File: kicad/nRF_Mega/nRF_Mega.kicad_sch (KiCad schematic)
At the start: 11 parts, among them J1 Screw_Terminal_01x02, M1 Motor_Servo, M2 Motor_Servo, M3 Motor_Servo, M4 Motor_Servo, M5 Motor_Servo, U1 NRF24L01_Breakout

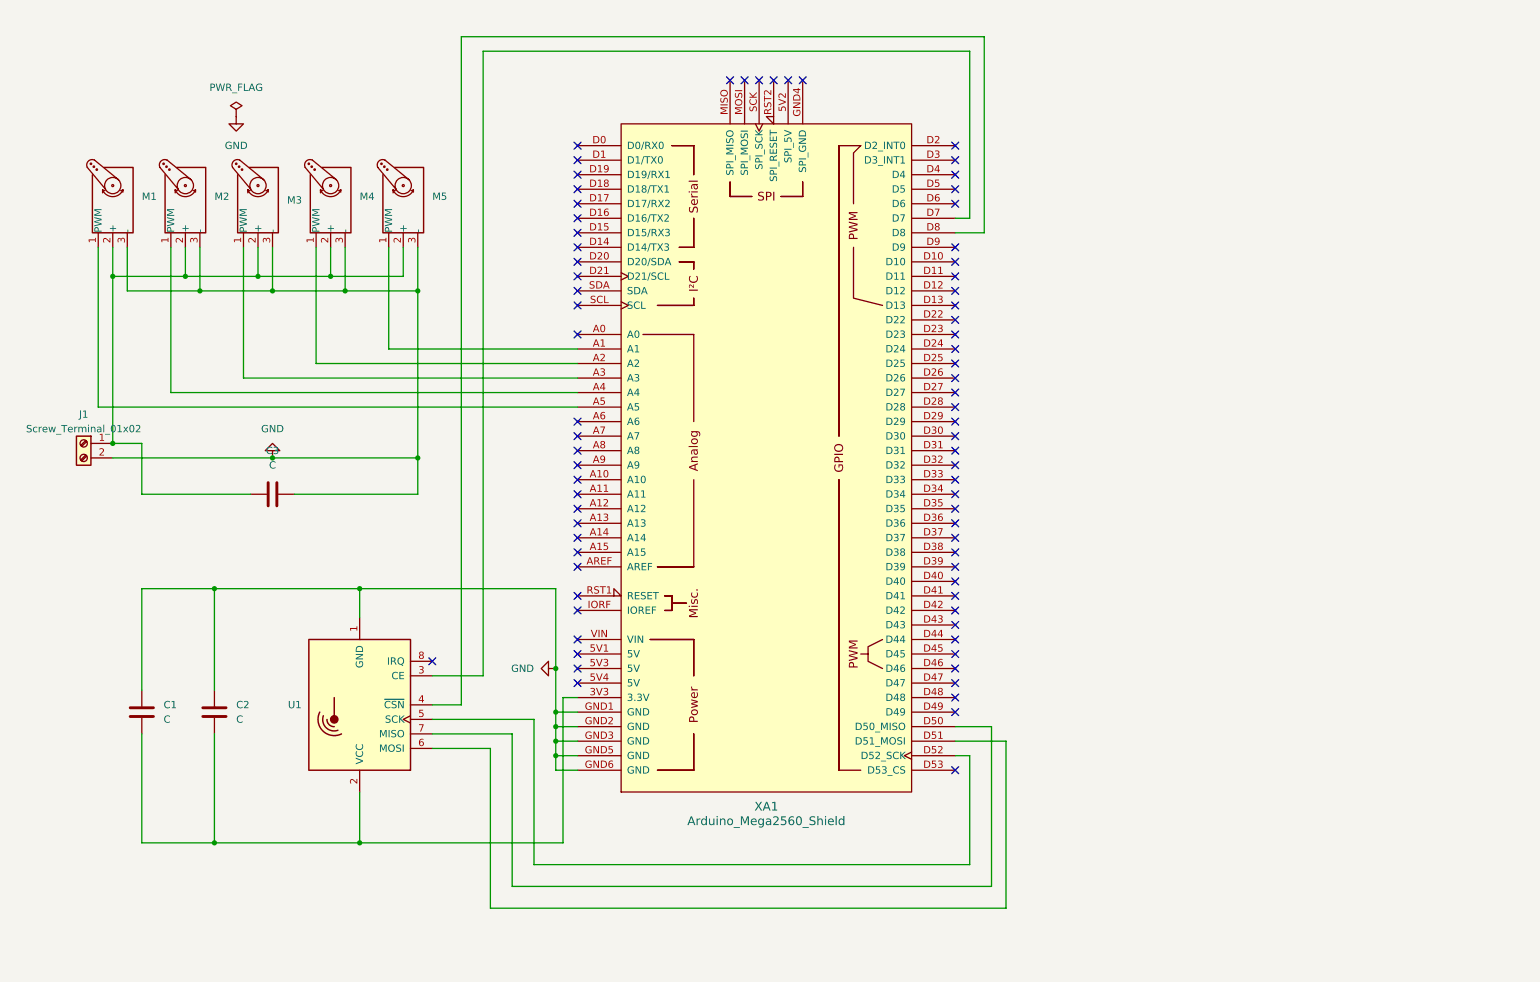
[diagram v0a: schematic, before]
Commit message: corrected nRF placement, minimized wire length, fixed caps and connector
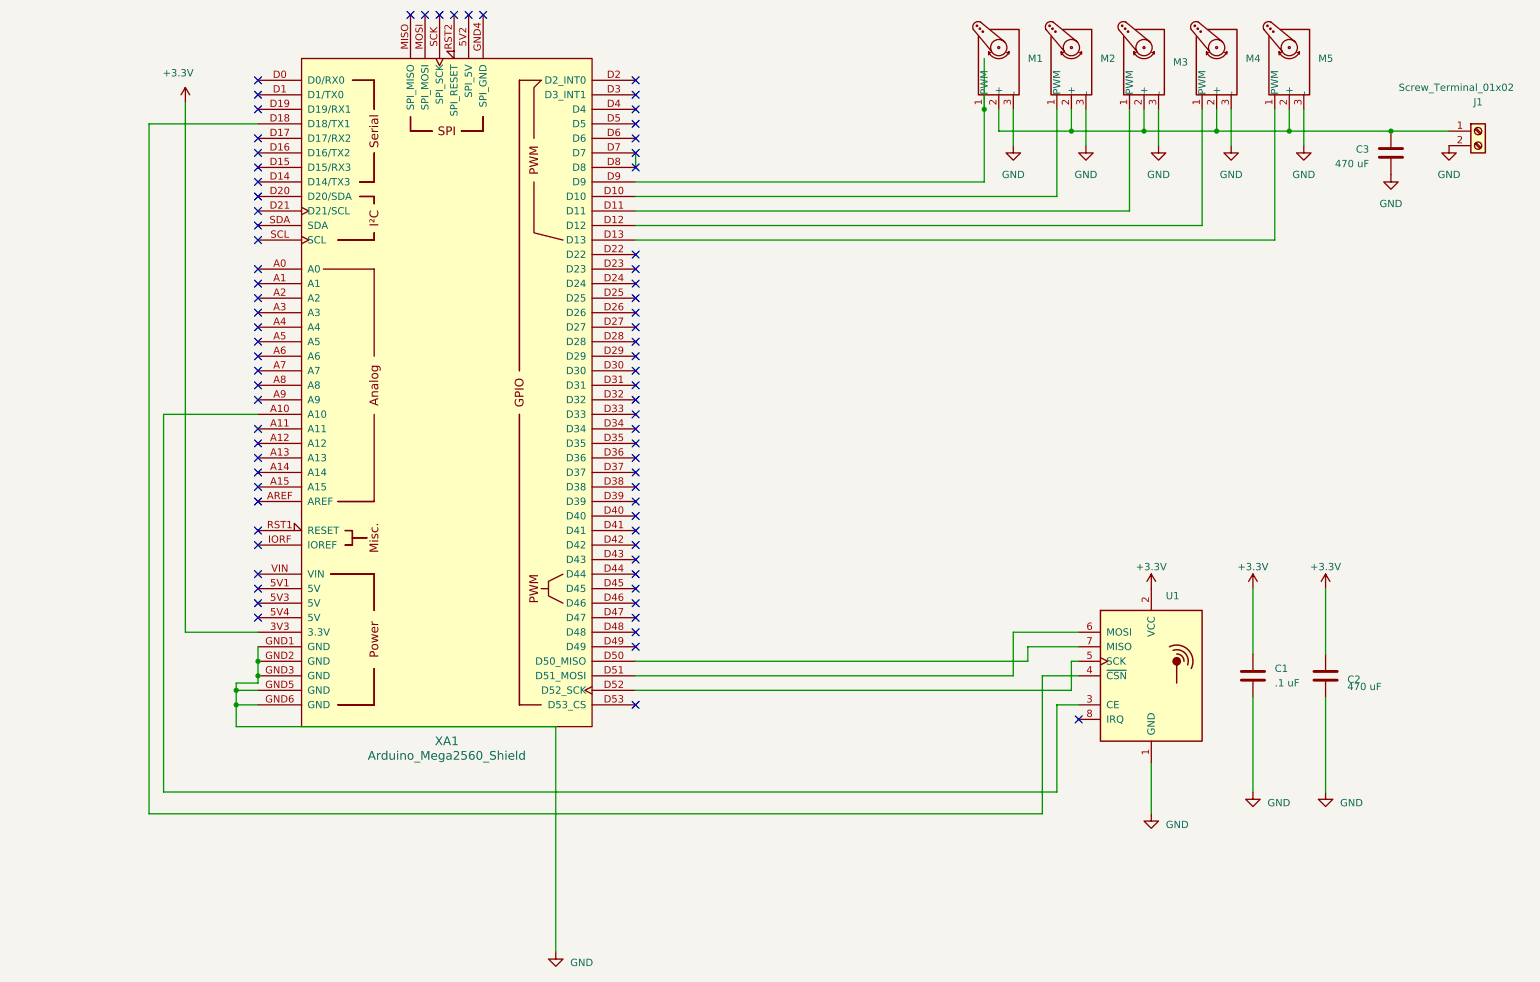
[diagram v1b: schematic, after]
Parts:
- C1: value C -> .1 uF; footprint Connector_PinHeader_2.54mm:PinHeader_1x02_P2.54mm_Vertical -> Capacitor_THT:C_Disc_D3.0mm_W1.6mm_P2.50mm
- C2, C3: value C -> 470 uF; footprint Connector_PinHeader_2.54mm:PinHeader_1x02_P2.54mm_Vertical -> Capacitor_THT:CP_Radial_D10.0mm_P5.00mm
- J1: footprint Connector_PinHeader_2.54mm:PinHeader_1x02_P2.54mm_Vertical -> TerminalBlock:TerminalBlock_bornier-2_P5.08mm
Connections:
- net GND: now also C1.2, C2.2; no longer C1.1, C2.1
- net at M4.1 (PWM): now also XA1.D12; no longer XA1.A2
- net at M5.1 (PWM): now also XA1.D13; no longer XA1.A1
- net +3.3V: now reaches U1.2 (VCC), XA1.3V3 (3.3V)
- net +3.3V: now also C1.1, C2.1; no longer C1.2, C2.2
- net at U1.3 (CE): now also XA1.A10; no longer XA1.D7
- net at U1.4 (~{CSN}): now also XA1.D18 (D18/TX1); no longer XA1.D8
- net at M2.1 (PWM): now also XA1.D10; no longer XA1.A4
- net at XA1.A3: no longer M3.1 (PWM)
- net at XA1.A5: no longer M1.1 (PWM)
- net at XA1.D11: now also M3.1 (PWM)
- net at XA1.D9: now also M1.1 (PWM)
- new net: XA1.D7, XA1.D8
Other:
- moved on the sheet: C1, C3, J1, M1, M2, M3, M4, M5, U1, XA1
